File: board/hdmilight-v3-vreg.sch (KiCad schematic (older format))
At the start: 44 parts, among them U12 TPS65266

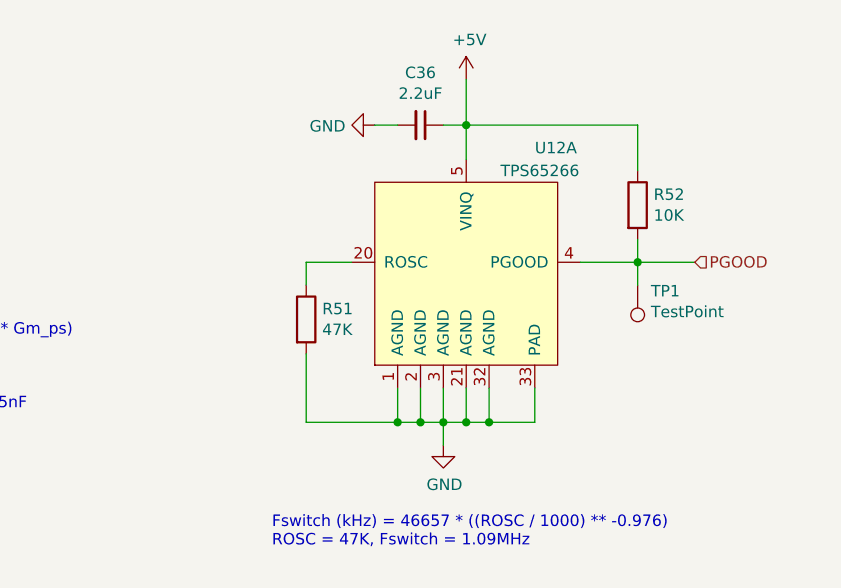
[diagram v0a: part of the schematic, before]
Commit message: Fixed bugs in v3.0 board:
 * Changed FPGA GPIO to 2 row with ground to make it compatible with logic analyser plug for debugging
 * Move position sensor from PB4 to PB5
 * Connect voltage regulator center pad to ground pins
 * Add SPI CS line between FPGA and MCU
 * Move HDMI hotplug LED back from board edge
 * Move HDMI ESD chip closer to connector
 * Swap serial rx/tx
 * Fix FPGA EEPROM footprint
 * Fix reset button footprint
 * Connect ADV I2C to MCU
 * Fix missing ground to hotplug power off circuit
 * Move LED power connector to back of board
 * Move standby button to front of board
 * Only use HDMI 5v for hotplug detect
 * Change LED power switching to high side to stop it grounding back through the data line
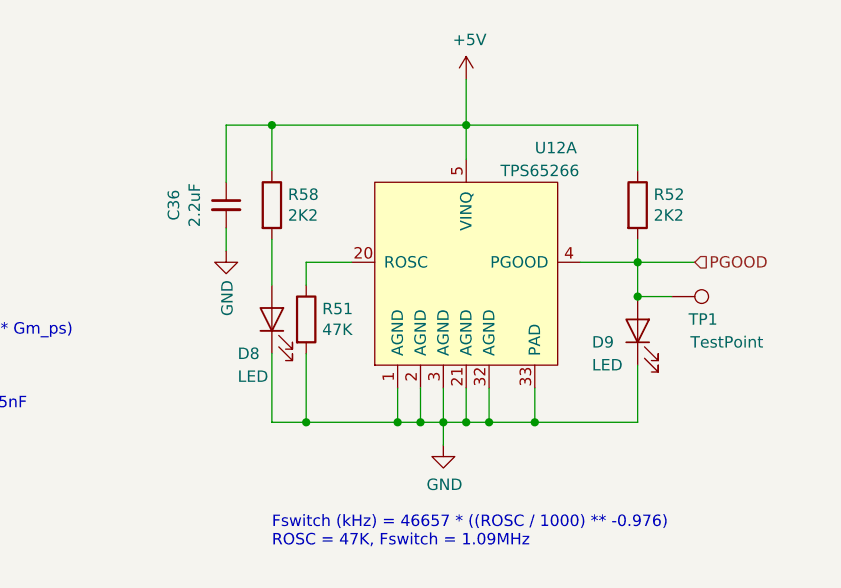
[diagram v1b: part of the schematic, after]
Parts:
- added D8, D9: LED, LED_SMD:LED_0603_1608Metric, symbol Device:LED
- added R58: 2K2, Resistor_SMD:R_0603_1608Metric, symbol Device:R
- R52: value 10K -> 2K2
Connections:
- net +5V: now also R58.1
- net GND: now also D8.1 (K), D9.1 (K)
- net PGOOD: now also D9.2 (A)
- new net: D8.2 (A), R58.2
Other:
- moved on the sheet: C36, TP1
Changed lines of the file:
@@
 L Device:C_Small C36
 U 1 1 5DE734DE
-P 9650 950
-F 0 "C36" V 9421 950 50  0000 C CNN
-F 1 "2.2uF" V 9512 950 50  0000 C CNN
-F 2 "Capacitor_SMD:C_0603_1608Metric" H 9650 950 50  0001 C CNN
-F 3 "~" H 9650 950 50  0001 C CNN
-	1    9650 950
-	0    1    1    0
-$EndComp
-Wire Wire Line
-	9750 950  9850 950
+P 8800 1300
+F 0 "C36" V 8571 1300 50  0000 C CNN
+F 1 "2.2uF" V 8662 1300 50  0000 C CNN
+F 2 "Capacitor_SMD:C_0603_1608Metric" H 8800 1300 50  0001 C CNN
+F 3 "~" H 8800 1300 50  0001 C CNN
+	1    8800 1300
+	1    0    0    -1
+$EndComp
 Wire Wire Line
 	9850 950  9850 1100
@@
 L power:GND #PWR0141
 U 1 1 5DE75CA5
-P 9450 950
-F 0 "#PWR0141" H 9450 700 50  0001 C CNN
-F 1 "GND" V 9455 822 50  0000 R CNN
-F 2 "" H 9450 950 50  0001 C CNN
-F 3 "" H 9450 950 50  0001 C CNN
-	1    9450 950
-	0    1    1    0
-$EndComp
-Wire Wire Line
-	9450 950  9550 950
+P 8800 1500
+F 0 "#PWR0141" H 8800 1250 50  0001 C CNN
+F 1 "GND" V 8805 1372 50  0000 R CNN
+F 2 "" H 8800 1500 50  0001 C CNN
+F 3 "" H 8800 1500 50  0001 C CNN
+	1    8800 1500
+	1    0    0    -1
+$EndComp
+Wire Wire Line
+	8800 1500 8800 1400
 $Comp
 L Device:R R52
@@
 P 10600 1300
 F 0 "R52" H 10670 1346 50  0000 L CNN
-F 1 "10K" H 10670 1255 50  0000 L CNN
+F 1 "2K2" H 10670 1255 50  0000 L CNN
 F 2 "Resistor_SMD:R_0603_1608Metric" V 10530 1300 50  0001 C CNN
 F 3 "~" H 10600 1300 50  0001 C CNN
@@
 L Connector:TestPoint TP1
 U 1 1 61BE6672
-P 10600 1650
-F 0 "TP1" H 10542 1676 50  0000 R CNN
-F 1 "TestPoint" H 10542 1767 50  0000 R CNN
-F 2 "TestPoint:TestPoint_Pad_D1.5mm" H 10800 1650 50  0001 C CNN
-F 3 "~" H 10800 1650 50  0001 C CNN
-	1    10600 1650
-	-1   0    0    1
-$EndComp
-Wire Wire Line
-	10600 1550 10600 1650
+P 10750 1700
+F 0 "TP1" V 10850 1900 50  0000 R CNN
+F 1 "TestPoint" V 10950 2100 50  0000 R CNN
+F 2 "TestPoint:TestPoint_Pad_D1.5mm" H 10950 1700 50  0001 C CNN
+F 3 "~" H 10950 1700 50  0001 C CNN
+	1    10750 1700
+	0    1    1    0
+$EndComp
 $Comp
 L Connector:TestPoint TP4
@@
 $EndComp
 Connection ~ 4400 6300
+$Comp
+L Device:LED D8
+U 1 1 5F278759
+P 9000 1800
+F 0 "D8" V 8850 1950 50  0000 R CNN
+F 1 "LED" V 8750 1950 50  0000 R CNN
+F 2 "LED_SMD:LED_0603_1608Metric" H 9000 1800 50  0001 C CNN
+F 3 "~" H 9000 1800 50  0001 C CNN
+	1    9000 1800
+	0    -1   -1   0
+$EndComp
+$Comp
+L Device:LED D9
+U 1 1 5F27A03E
+P 10600 1850
+F 0 "D9" V 10550 2050 50  0000 R CNN
+F 1 "LED" V 10450 2050 50  0000 R CNN
+F 2 "LED_SMD:LED_0603_1608Metric" H 10600 1850 50  0001 C CNN
+F 3 "~" H 10600 1850 50  0001 C CNN
+	1    10600 1850
+	0    -1   -1   0
+$EndComp
+$Comp
+L Device:R R58
+U 1 1 5F27A8CD
+P 9000 1300
+F 0 "R58" H 9070 1346 50  0000 L CNN
+F 1 "2K2" H 9070 1255 50  0000 L CNN
+F 2 "Resistor_SMD:R_0603_1608Metric" V 8930 1300 50  0001 C CNN
+F 3 "~" H 9000 1300 50  0001 C CNN
+	1    9000 1300
+	1    0    0    -1
+$EndComp
+Wire Wire Line
+	9000 1450 9000 1650
+Wire Wire Line
+	9000 1950 9000 2250
+Wire Wire Line
+	9000 2250 9150 2250
+Connection ~ 9150 2250
+Wire Wire Line
+	9000 1150 9000 950
+Wire Wire Line
+	9000 950  9850 950
+Wire Wire Line
+	8800 950  9000 950
+Wire Wire Line
+	8800 950  8800 1200
+Connection ~ 9000 950
+Wire Wire Line
+	10750 1700 10600 1700
+Wire Wire Line
+	10600 1550 10600 1700
+Connection ~ 10600 1700
+Wire Wire Line
+	10150 2250 10600 2250
+Wire Wire Line
+	10600 2250 10600 2000
+Connection ~ 10150 2250
 $EndSCHEMATC

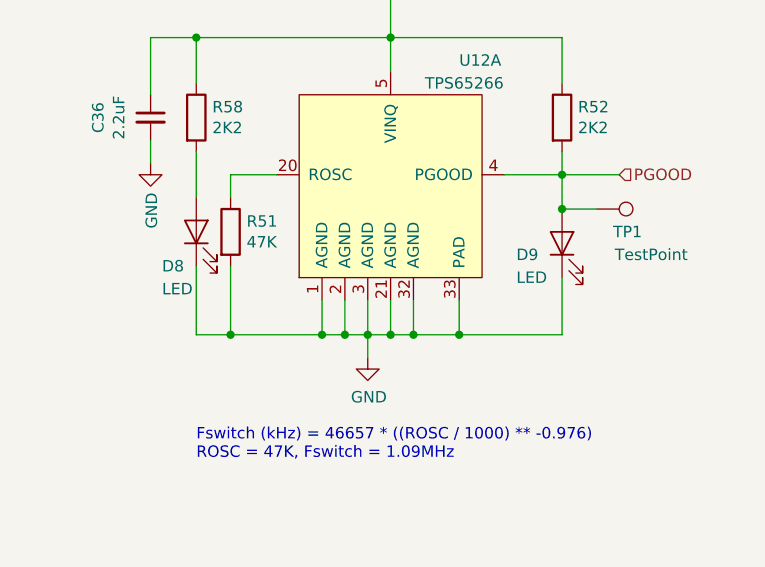
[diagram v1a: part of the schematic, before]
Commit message: Updated BOM with individual LED colours/types
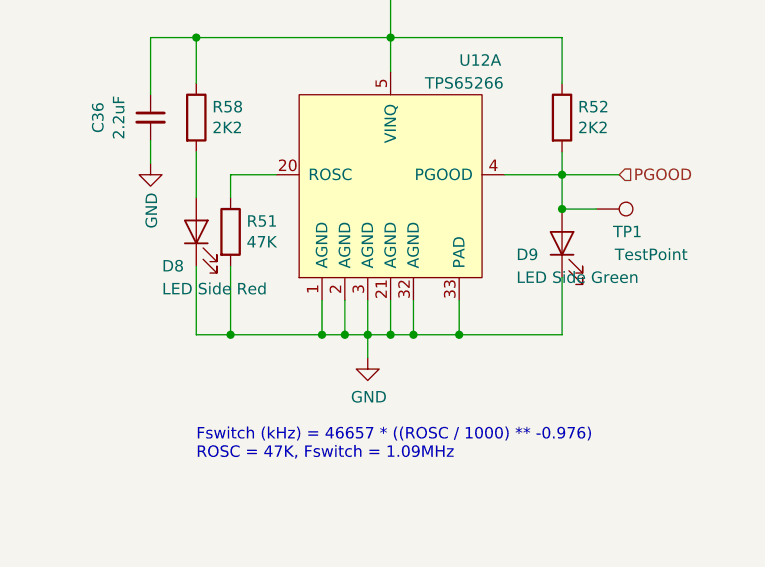
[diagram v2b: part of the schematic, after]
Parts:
- D8: value LED -> LED Side Red
- D9: value LED -> LED Side Green
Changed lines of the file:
@@
 P 9000 1800
 F 0 "D8" V 8850 1950 50  0000 R CNN
-F 1 "LED" V 8750 1950 50  0000 R CNN
+F 1 "LED Side Red" V 8750 1950 50  0000 R CNN
 F 2 "LED_SMD:LED_0603_1608Metric" H 9000 1800 50  0001 C CNN
 F 3 "~" H 9000 1800 50  0001 C CNN
@@
 P 10600 1850
 F 0 "D9" V 10550 2050 50  0000 R CNN
-F 1 "LED" V 10450 2050 50  0000 R CNN
+F 1 "LED Side Green" V 10450 2050 50  0000 R CNN
 F 2 "LED_SMD:LED_0603_1608Metric" H 10600 1850 50  0001 C CNN
 F 3 "~" H 10600 1850 50  0001 C CNN
